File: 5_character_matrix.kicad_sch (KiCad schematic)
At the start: 19 parts, among them U1 LSHD-5503, U19 SN74LVC244A, U2 LSHD-5503, U3 LSHD-5503, U4 LSHD-5503, U6 LSHD-5503, U7 SN74LVC244A

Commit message: change in display module
- Created new sheets
- Reordered the sheets
- Created the footprint for the display
- 3D model of the display
- MCU selection
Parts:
- removed C2, C3: 10u, symbol Device:C
- removed U1, U2, U3, U4, U6: LSHD-5503, symbol precision_clock:LSHD-5503
- added U1, U10, U14, U18, U6: SC10-21SURKWA, precision_clock:SC10-21SURKWA, symbol precision_clock:SC10-21SURKWA
- U2: renamed from U19; footprint (none) -> Package_SO:TSSOP-20_4.4x6.5mm_P0.65mm
- U5: renamed from U7; footprint (none) -> Package_SO:TSSOP-20_4.4x6.5mm_P0.65mm
- renumbered C15 to C1, C4 to C2, R26 to R1
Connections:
- net BA0: now also U1.7 (A), U10.7 (A), U14.7 (A), U18.7 (A), U6.7 (A)
- net BA1: now also U1.6 (B), U10.6 (B), U14.6 (B), U6.6 (B)
- net BA2: now also U1.4 (C), U10.4 (C), U14.4 (C), U18.4 (C), U18.6 (B), U6.4 (C)
- net BA3: now also U1.2 (D), U10.2 (D), U14.2 (D), U18.2 (D), U6.2 (D)
- net BA4: now also U1.1 (E), U10.1 (E), U14.1 (E), U18.1 (E), U6.1 (E)
- net BA5: now also U1.9 (F), U10.9 (F), U14.9 (F), U18.9 (F), U6.9 (F)
- net BA6: now also U1.10 (G), U10.10 (G), U14.10 (G), U18.10 (G), U6.10 (G)
- net BA7: now also U1.5 (DP), U10.5 (DP), U14.5 (DP), U18.5 (DP), U6.5 (DP)
- net BK0: now also U1.3 (CC), U1.8 (CC)
- net BK1: now also U6.3 (CC), U6.8 (CC)
- net BK2: now also U10.3 (CC), U10.8 (CC)
- net BK3: now also U14.3 (CC), U14.8 (CC)
- net BK4: now also U18.3 (CC), U18.8 (CC)
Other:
- note added: "KingBright forwards voltage is above the 3.3V drive voltage of the buffers take a look at this buffer chip MC74VHC541"

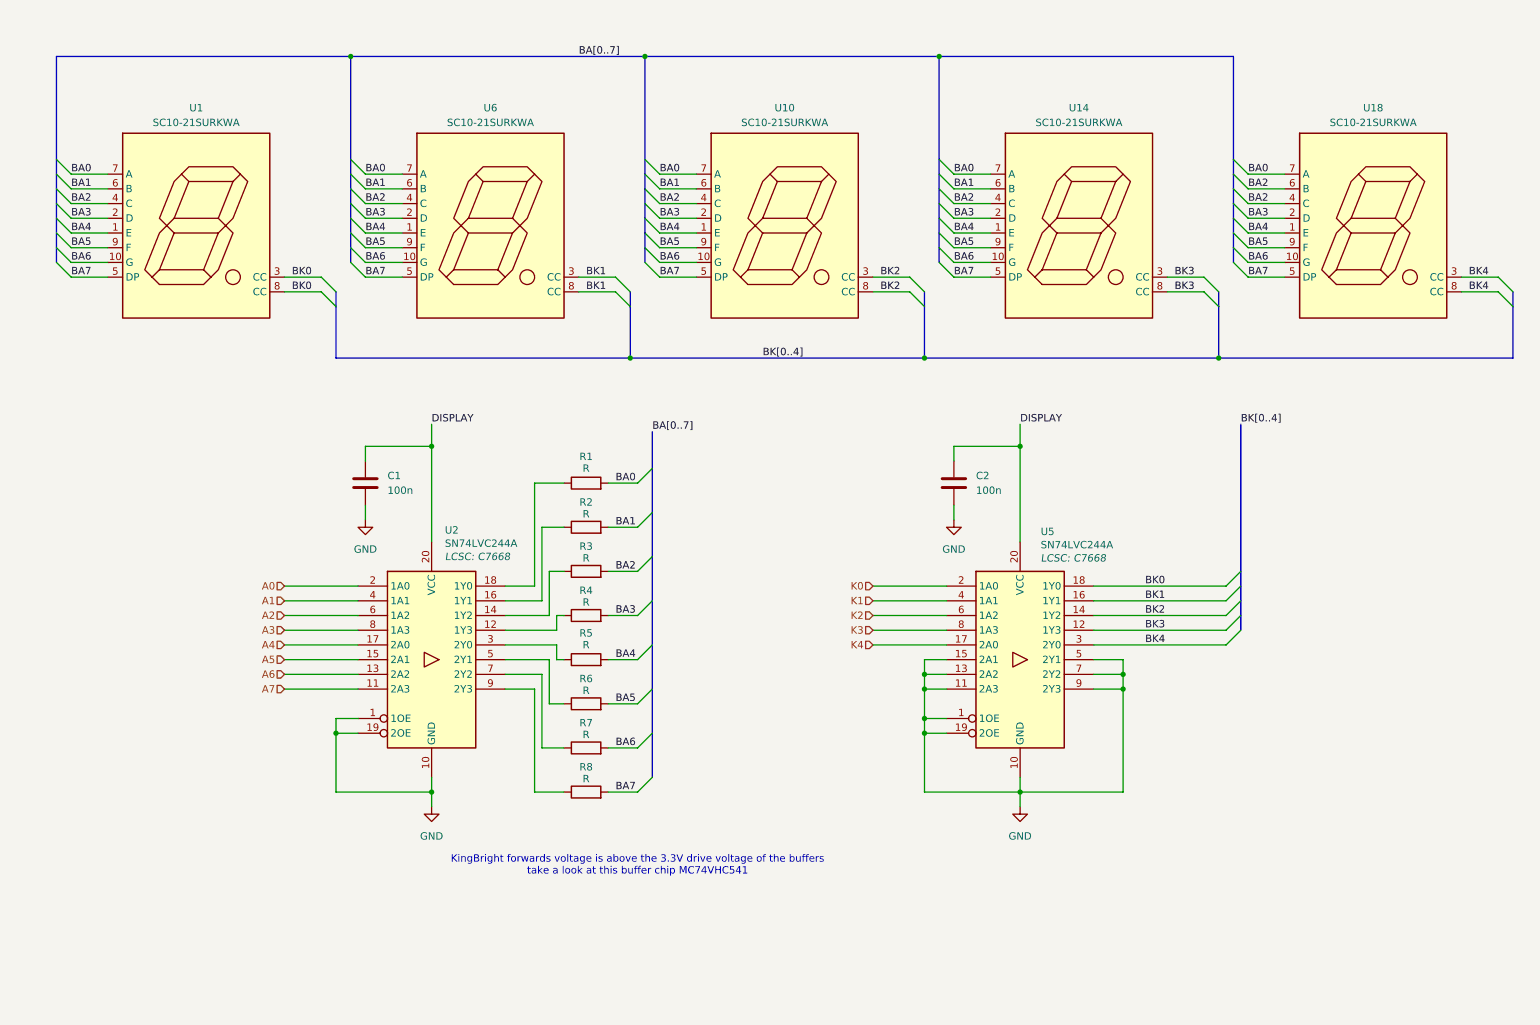
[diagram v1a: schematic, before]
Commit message: change in display module
- changes the display to a common anode type display
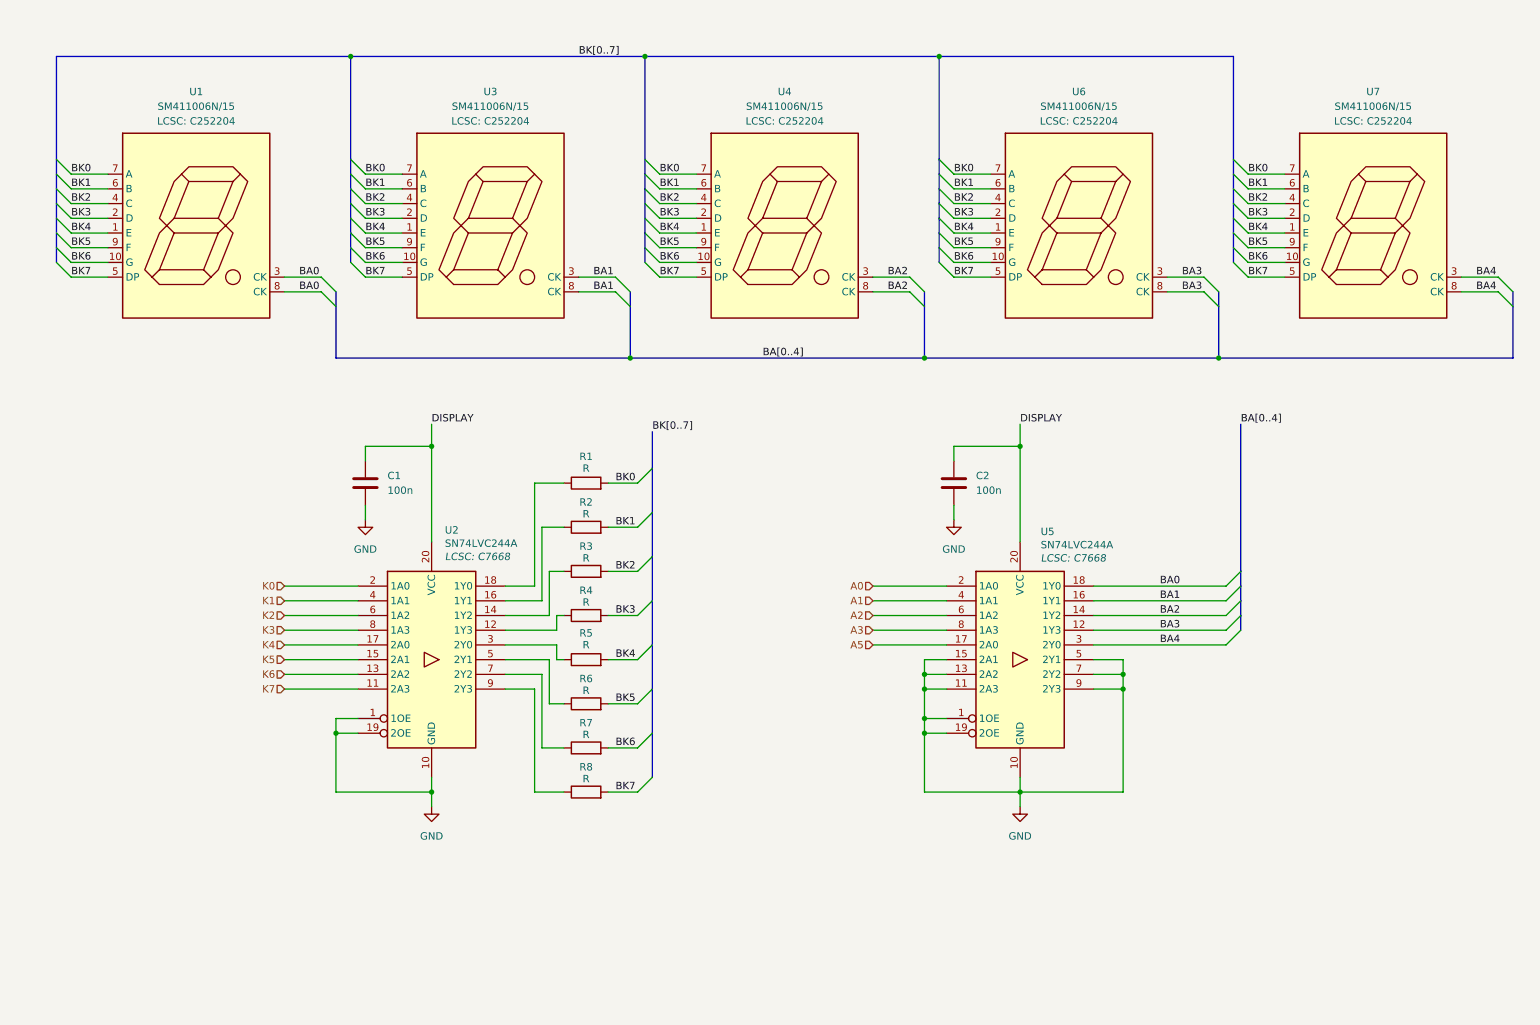
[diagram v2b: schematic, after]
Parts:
- removed U1, U10, U14, U18, U6: SC10-21SURKWA, precision_clock:SC10-21SURKWA, symbol precision_clock:SC10-21SURKWA
- added U1, U3, U4, U6, U7: SM411006N/15, precision_clock:SM411006N15, symbol precision_clock:SM411006N/15
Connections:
- net A4 is gone; now on net K4: U2.17 (2A0)
- net A0: now also U5.2 (1A0); no longer U2.2 (1A0)
- net A1: now also U5.4 (1A1); no longer U2.4 (1A1)
- net A2: now also U5.6 (1A2); no longer U2.6 (1A2)
- net A3: now also U5.8 (1A3); no longer U2.8 (1A3)
- net A5: now also U5.17 (2A0); no longer U2.15 (2A1)
- net BA0: now also U5.18 (1Y0), U1.3 (CK), U1.8 (CK); no longer R1.2
- net BA1: now also U5.16 (1Y1), U3.3 (CK), U3.8 (CK); no longer R2.2
- net BA2: now also U5.14 (1Y2), U4.3 (CK), U4.8 (CK); no longer R3.2
- net BA3: now also U5.12 (1Y3), U6.3 (CK), U6.8 (CK); no longer R4.2
- net BA4: now also U5.3 (2Y0), U7.3 (CK), U7.8 (CK); no longer R5.2
- net BK0: now also R1.2, U1.7 (A), U3.7 (A), U4.7 (A), U6.7 (A), U7.7 (A); no longer U5.18 (1Y0)
- net BK1: now also R2.2, U1.6 (B), U3.6 (B), U4.6 (B), U6.6 (B), U7.6 (B); no longer U5.16 (1Y1)
- net BK2: now also R3.2, U1.4 (C), U3.4 (C), U4.4 (C), U6.4 (C), U7.4 (C); no longer U5.14 (1Y2)
- net BK3: now also R4.2, U1.2 (D), U3.2 (D), U4.2 (D), U6.2 (D), U7.2 (D); no longer U5.12 (1Y3)
- net BK4: now also R5.2, U1.1 (E), U3.1 (E), U4.1 (E), U6.1 (E), U7.1 (E); no longer U5.3 (2Y0)
- net K0: now also U2.2 (1A0); no longer U5.2 (1A0)
- net K1: now also U2.4 (1A1); no longer U5.4 (1A1)
- net K2: now also U2.6 (1A2); no longer U5.6 (1A2)
- net K3: now also U2.8 (1A3); no longer U5.8 (1A3)
- net K4: no longer U5.17 (2A0)
- net A6 renamed K6
- net A7 renamed K7
- net BA5 renamed BK5
- net BK5: now also U1.9 (F), U3.9 (F), U4.9 (F), U6.9 (F), U7.9 (F)
- net BA6 renamed BK6
- net BK6: now also U1.10 (G), U3.10 (G), U4.10 (G), U6.10 (G), U7.10 (G)
- net BA7 renamed BK7
- net BK7: now also U1.5 (DP), U3.5 (DP), U4.5 (DP), U6.5 (DP), U7.5 (DP)
- new net K5: U2.15 (2A1)
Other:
- note removed: "KingBright forwards voltage is above the 3.3V drive voltage of the buffers take a look at this buffer chip MC74VHC541"

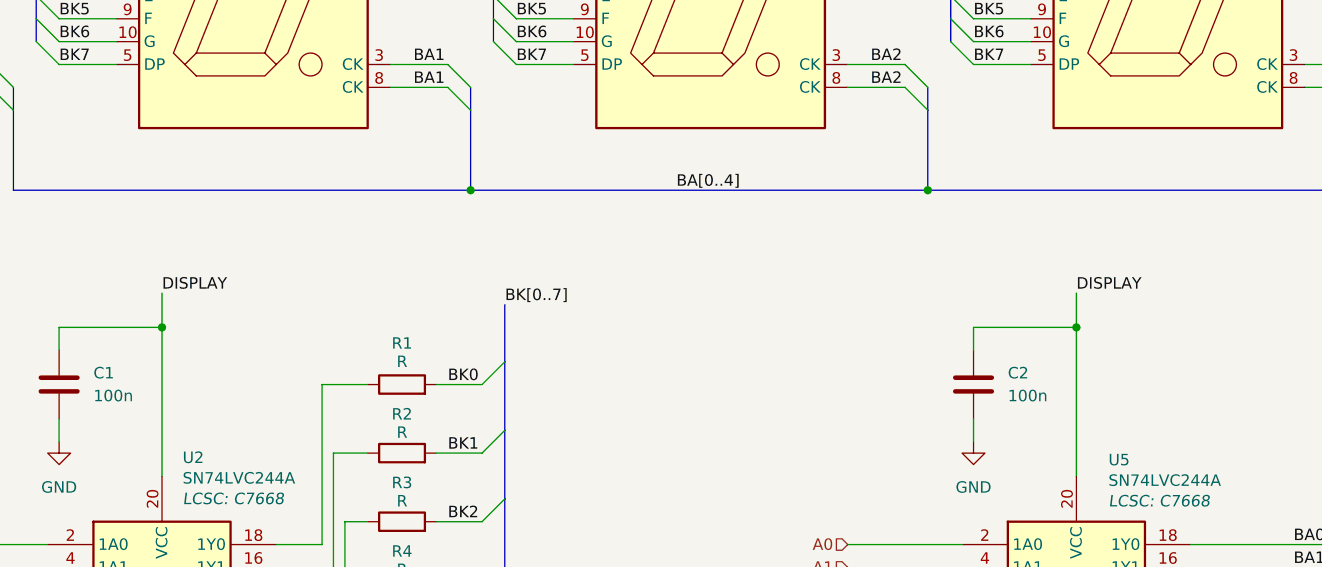
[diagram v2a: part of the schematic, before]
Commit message: primary MCU changes
- added preliminary decoupling
- added LSE
- added flash memory
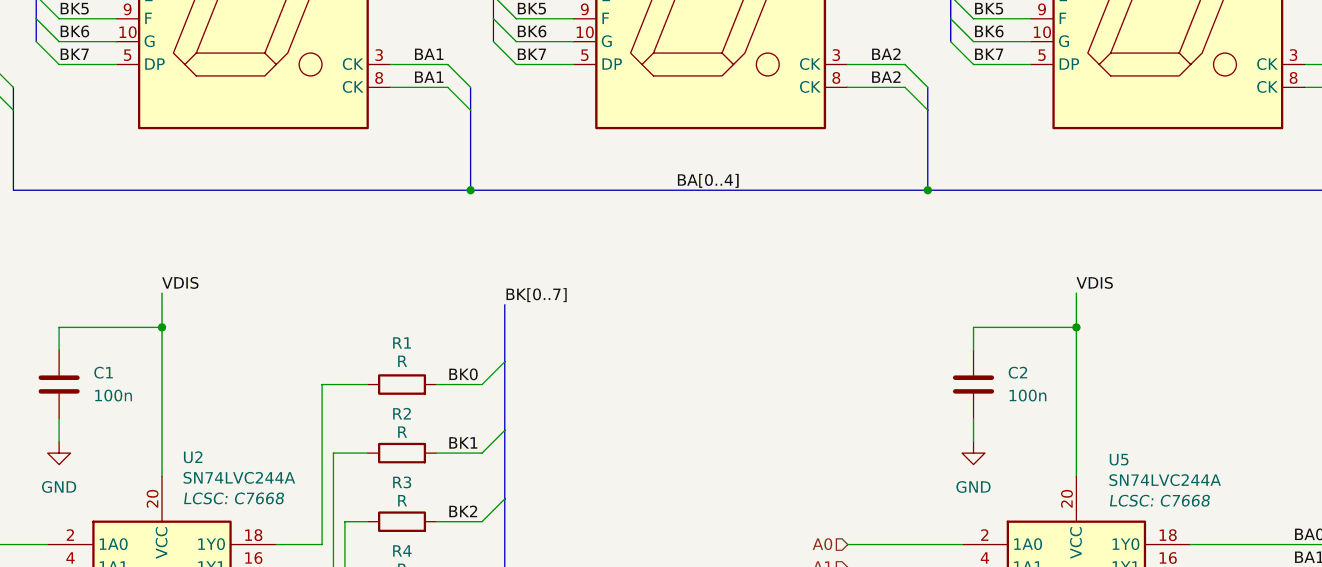
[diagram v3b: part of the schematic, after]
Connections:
- net DISPLAY renamed VDIS
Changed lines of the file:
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@@
 		)
 	)
-	(label "DISPLAY"
+	(label "VDIS"
 		(at 191.77 88.9 0)
 		(effects
@@
 		)
 	)
-	(label "DISPLAY"
+	(label "VDIS"
 		(at 90.17 88.9 0)
 		(effects

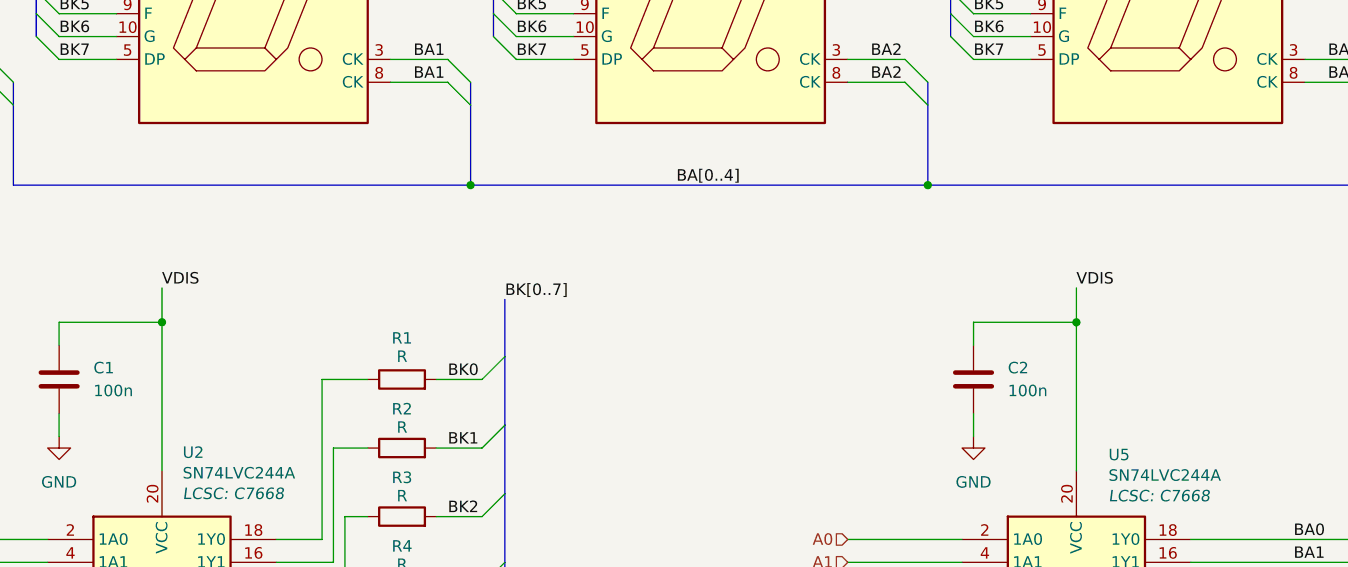
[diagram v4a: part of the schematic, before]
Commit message: minor changes
- removed the power, ambient light sensing circuits.
- minor changes in the primary MCU pinout.
- USB connector moved to MCU sheet.
- ESD protection added.
- removed the test points from the individual sheets.
- Improved readability.
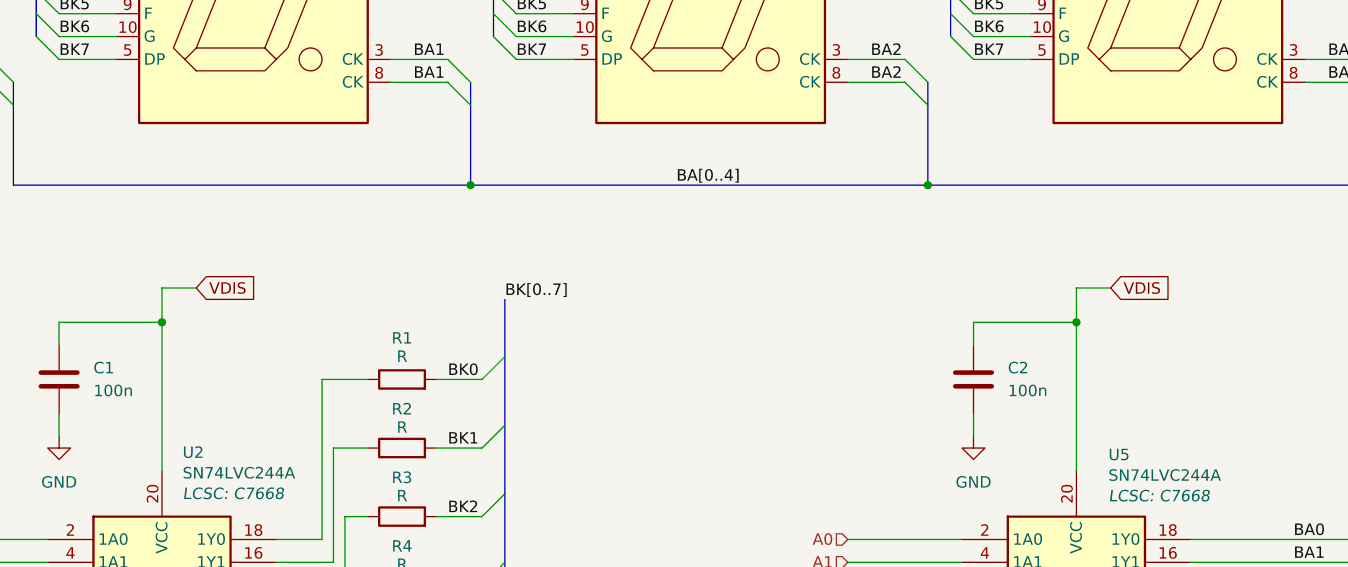
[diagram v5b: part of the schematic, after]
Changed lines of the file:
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@@
 	)
 	(junction
-		(at 191.77 92.71)
-		(diameter 0)
-		(color 0 0 0 0)
-	)
-	(junction
 		(at 124.46 77.47)
 		(diameter 0)
@@
 	)
 	(junction
+		(at 191.77 92.71)
+		(diameter 0)
+		(color 0 0 0 0)
+	)
+	(junction
 		(at 90.17 152.4)
 		(diameter 0)
@@
 	(wire
 		(pts
-			(xy 191.77 88.9) (xy 191.77 92.71)
-		)
-		(stroke
-			(width 0)
-			(type default)
-		)
-	)
-	(wire
-		(pts
 			(xy 166.37 121.92) (xy 179.07 121.92)
 		)
@@
 		)
 	)
+	(wire
+		(pts
+			(xy 191.77 88.9) (xy 191.77 92.71)
+		)
+		(stroke
+			(width 0)
+			(type default)
+		)
+	)
 	(bus
 		(pts
@@
 	(wire
 		(pts
+			(xy 195.58 88.9) (xy 191.77 88.9)
+		)
+		(stroke
+			(width 0)
+			(type default)
+		)
+	)
+	(wire
+		(pts
 			(xy 64.77 119.38) (xy 77.47 119.38)
 		)
@@
 	(wire
 		(pts
+			(xy 90.17 88.9) (xy 90.17 92.71)
+		)
+		(stroke
+			(width 0)
+			(type default)
+		)
+	)
+	(wire
+		(pts
 			(xy 231.14 55.88) (xy 237.49 55.88)
 		)
@@
 	(wire
 		(pts
+			(xy 93.98 88.9) (xy 90.17 88.9)
+		)
+		(stroke
+			(width 0)
+			(type default)
+		)
+	)
+	(wire
+		(pts
 			(xy 231.14 50.8) (xy 237.49 50.8)
 		)
@@
 	(wire
 		(pts
-			(xy 90.17 88.9) (xy 90.17 92.71)
-		)
-		(stroke
-			(width 0)
-			(type default)
-		)
-	)
-	(wire
-		(pts
 			(xy 120.65 152.4) (xy 125.73 152.4)
 		)
@@
 		)
 	)
-	(label "VDIS"
-		(at 191.77 88.9 0)
-		(effects
-			(font
-				(size 1.27 1.27)
-			)
-			(justify left bottom)
-		)
-	)
 	(label "BA[0..4]"
 		(at 229.87 88.9 0)
@@
 		)
 	)
-	(label "VDIS"
-		(at 90.17 88.9 0)
+	(label "BA3"
+		(at 219.71 63.5 0)
 		(effects
 			(font
@@
 		)
 	)
-	(label "BA3"
-		(at 219.71 63.5 0)
+	(global_label "VDIS"
+		(shape input)
+		(at 195.58 88.9 0)
+		(fields_autoplaced yes)
 		(effects
 			(font
 				(size 1.27 1.27)
 			)
-			(justify left bottom)
+			(justify left)
+		)
+		(property "Intersheetrefs" "${INTERSHEET_REFS}"
+			(at 202.7381 88.9 0)
+			(effects
+				(font
+					(size 1.27 1.27)
+				)
+				(justify left)
+				(hide yes)
+			)
+		)
+	)
+	(global_label "VDIS"
+		(shape input)
+		(at 93.98 88.9 0)
+		(fields_autoplaced yes)
+		(effects
+			(font
+				(size 1.27 1.27)
+			)
+			(justify left)
+		)
+		(property "Intersheetrefs" "${INTERSHEET_REFS}"
+			(at 101.1381 88.9 0)
+			(effects
+				(font
+					(size 1.27 1.27)
+				)
+				(justify left)
+				(hide yes)
+			)
 		)
 	)
